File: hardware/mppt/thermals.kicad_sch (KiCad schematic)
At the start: 27 parts, among them J401 Conn_01x04, J402 Conn_01x03, U401 MCP9700Ax-ELT, U402 MCP9700Ax-ELT

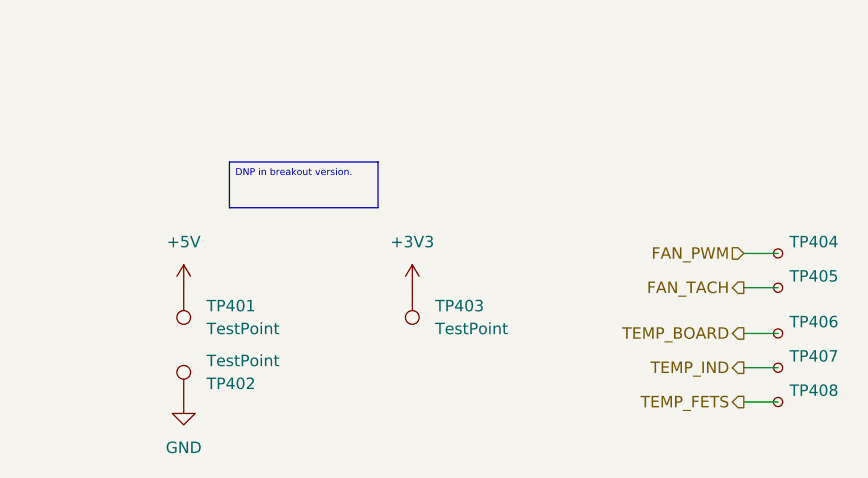
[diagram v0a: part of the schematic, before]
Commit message: remove testpoints, integrat 60% of layout
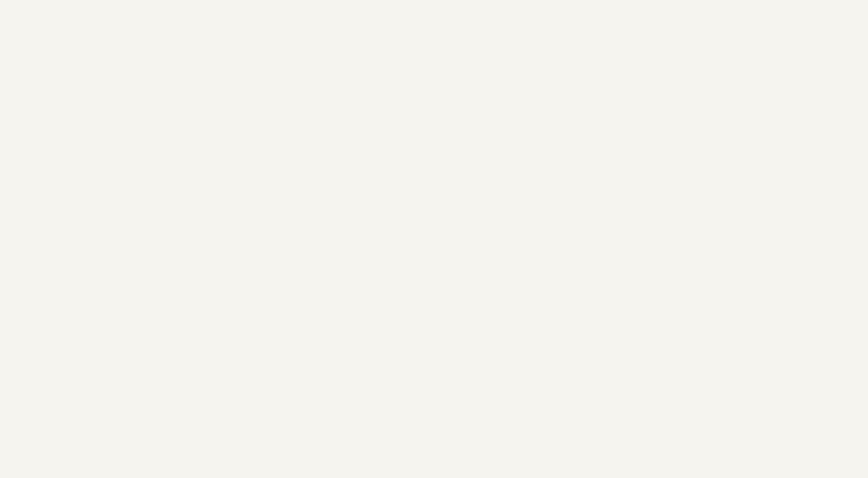
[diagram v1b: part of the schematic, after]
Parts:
- removed TP401, TP402, TP403: TestPoint, TestPoint:TestPoint_Keystone_5000-5004_Miniature, symbol Connector:TestPoint
- removed TP404, TP405, TP406, TP407, TP408: TestPoint_Small, TestPoint:TestPoint_Pad_D1.0mm, symbol Connector:TestPoint_Small
